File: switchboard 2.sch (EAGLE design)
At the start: 214 parts, among them IC1 MT8816AP, IC10 Z8F2480SO, IC11 LMV321M5, IC12 74HC595D, IC14 74LVC1G125DBV, IC15 74LVC1G125DBV, IC16 LM2940-9, IC17 PC817S OPTO, IC2 NE5532D, IC3 TC7660-SOIC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

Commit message: Layout development.
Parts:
- R14, R16, R18, R19, R2, R24, R3, R7: value 1M SMD -> 1M
- R17, R23, R25, R4: value 1k SMD -> 1k
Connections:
- new net N$83: IC14A.O, R60.1, SJ3.1
- net UART_RX: no longer IC14A.O, R60.1, SJ3.1
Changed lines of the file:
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@@
 <part name="GND2" library="supply1" deviceset="GND" device=""/>
 <part name="IC9" library="linear" deviceset="NE5532" device="D" value="NE5532D"/>
-<part name="R2" library="rcl" deviceset="R-US_" device="R0603" value="1M SMD"/>
-<part name="R3" library="rcl" deviceset="R-US_" device="R0603" value="1M SMD"/>
-<part name="R4" library="rcl" deviceset="R-US_" device="R0603" value="1k SMD"/>
+<part name="R2" library="rcl" deviceset="R-US_" device="R0603" value="1M"/>
+<part name="R3" library="rcl" deviceset="R-US_" device="R0603" value="1M"/>
+<part name="R4" library="rcl" deviceset="R-US_" device="R0603" value="1k"/>
 <part name="GND5" library="supply1" deviceset="GND" device=""/>
 <part name="GND6" library="supply1" deviceset="GND" device=""/>
@@
 <part name="R6" library="rcl" deviceset="R-US_" device="R0805" value="1k SMD"/>
 <part name="GND7" library="supply1" deviceset="GND" device=""/>
-<part name="R7" library="rcl" deviceset="R-US_" device="R0603" value="1M SMD"/>
-<part name="R24" library="rcl" deviceset="R-US_" device="R0603" value="1M SMD"/>
+<part name="R7" library="rcl" deviceset="R-US_" device="R0603" value="1M"/>
+<part name="R24" library="rcl" deviceset="R-US_" device="R0603" value="1M"/>
 <part name="GND50" library="supply1" deviceset="GND" device=""/>
-<part name="R25" library="rcl" deviceset="R-US_" device="R0603" value="1k SMD"/>
+<part name="R25" library="rcl" deviceset="R-US_" device="R0603" value="1k"/>
 <part name="C7" library="rcl" deviceset="C-EU" device="C0603" value="100n"/>
 <part name="R34" library="rcl" deviceset="R-US_" device="R0805" value="100"/>
@@
 <part name="R15" library="rcl" deviceset="R-US_" device="R0805" value="10k"/>
 <part name="IC2" library="linear" deviceset="NE5532" device="D" value="NE5532D"/>
-<part name="R14" library="rcl" deviceset="R-US_" device="R0603" value="1M SMD"/>
-<part name="R16" library="rcl" deviceset="R-US_" device="R0603" value="1M SMD"/>
-<part name="R17" library="rcl" deviceset="R-US_" device="R0603" value="1k SMD"/>
+<part name="R14" library="rcl" deviceset="R-US_" device="R0603" value="1M"/>
+<part name="R16" library="rcl" deviceset="R-US_" device="R0603" value="1M"/>
+<part name="R17" library="rcl" deviceset="R-US_" device="R0603" value="1k"/>
 <part name="GND16" library="supply1" deviceset="GND" device=""/>
 <part name="GND19" library="supply1" deviceset="GND" device=""/>
-<part name="R18" library="rcl" deviceset="R-US_" device="R0603" value="1M SMD"/>
-<part name="R19" library="rcl" deviceset="R-US_" device="R0603" value="1M SMD"/>
+<part name="R18" library="rcl" deviceset="R-US_" device="R0603" value="1M"/>
+<part name="R19" library="rcl" deviceset="R-US_" device="R0603" value="1M"/>
 <part name="GND20" library="supply1" deviceset="GND" device=""/>
-<part name="R23" library="rcl" deviceset="R-US_" device="R0603" value="1k SMD"/>
+<part name="R23" library="rcl" deviceset="R-US_" device="R0603" value="1k"/>
 <part name="C14" library="rcl" deviceset="C-EU" device="C0603" value="100n"/>
 <part name="P_INPUT2" library="pinhead" deviceset="PINHD-1X2" device=""/>
@@
 </segment>
 <segment>
-<wire x1="-347.98" y1="233.68" x2="-342.9" y2="233.68" width="0.1524" layer="91"/>
-<pinref part="IC14" gate="A" pin="O"/>
-<pinref part="SJ3" gate="G$1" pin="1"/>
-<wire x1="-342.9" y1="193.04" x2="-342.9" y2="233.68" width="0.1524" layer="91"/>
-<pinref part="R60" gate="G$1" pin="1"/>
-<wire x1="-335.28" y1="233.68" x2="-342.9" y2="233.68" width="0.1524" layer="91"/>
-<junction x="-342.9" y="233.68"/>
-</segment>
-<segment>
 <pinref part="R60" gate="G$1" pin="2"/>
 <wire x1="-325.12" y1="233.68" x2="-317.5" y2="233.68" width="0.1524" layer="91"/>
@@
 </segment>
 </net>
+<net name="N$83" class="0">
+<segment>
+<pinref part="IC14" gate="A" pin="O"/>
+<pinref part="R60" gate="G$1" pin="1"/>
+<wire x1="-347.98" y1="233.68" x2="-342.9" y2="233.68" width="0.1524" layer="91"/>
+<pinref part="SJ3" gate="G$1" pin="1"/>
+<wire x1="-342.9" y1="233.68" x2="-335.28" y2="233.68" width="0.1524" layer="91"/>
+<wire x1="-342.9" y1="193.04" x2="-342.9" y2="233.68" width="0.1524" layer="91"/>
+<junction x="-342.9" y="233.68"/>
+</segment>
+</net>

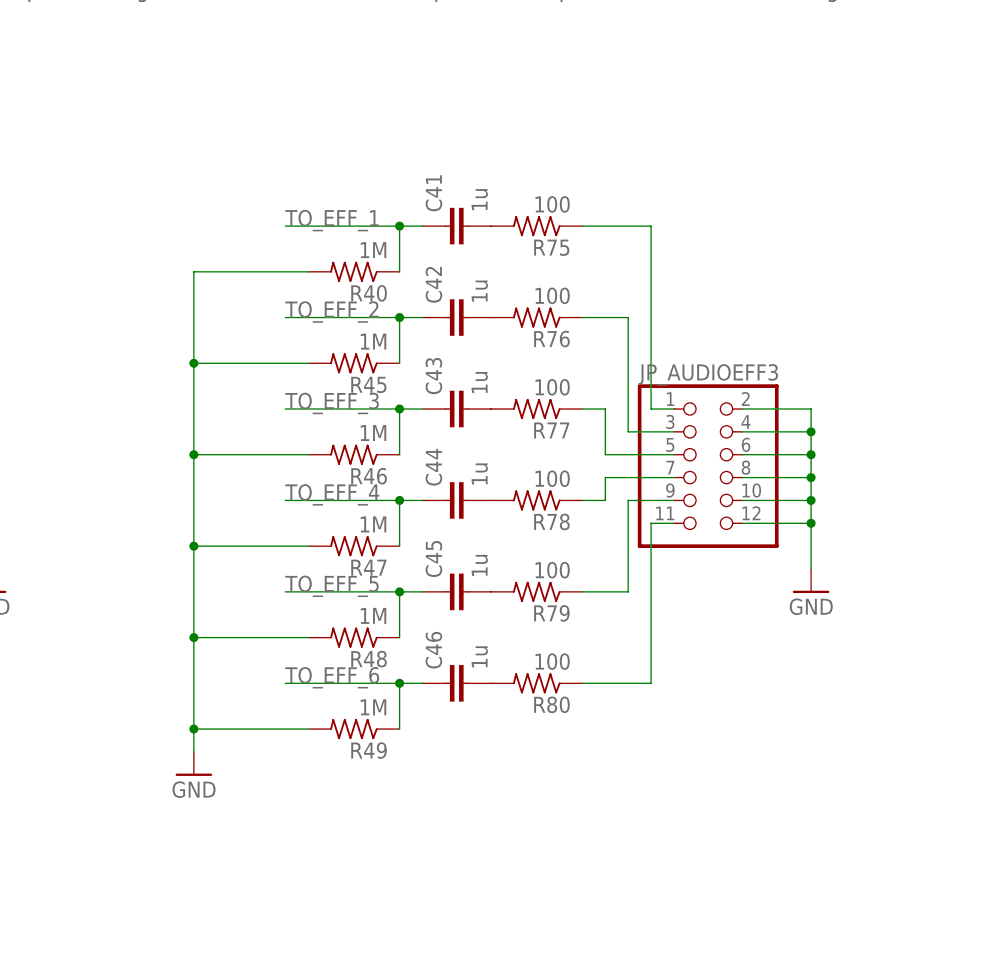
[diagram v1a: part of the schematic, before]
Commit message: Layout development. Board dimensions changed.
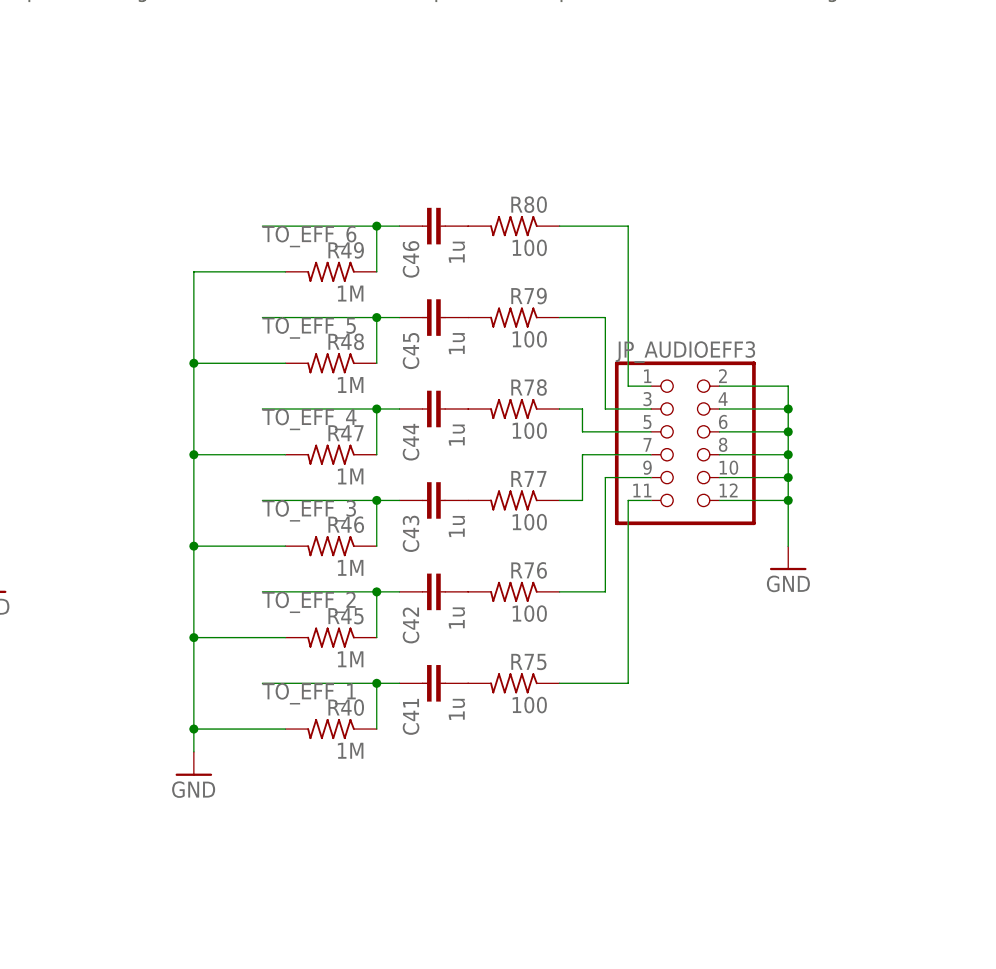
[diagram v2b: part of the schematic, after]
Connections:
- net N$21: now also JP_AUDIOEFF3.11; no longer JP_AUDIOEFF3.1
- net N$32: now also JP_AUDIOEFF3.9; no longer JP_AUDIOEFF3.3
- net N$52: now also JP_AUDIOEFF3.7; no longer JP_AUDIOEFF3.5
- net N$53: now also JP_AUDIOEFF3.5; no longer JP_AUDIOEFF3.7
- net N$59: now also JP_AUDIOEFF3.3; no longer JP_AUDIOEFF3.9
- net N$62: now also JP_AUDIOEFF3.1; no longer JP_AUDIOEFF3.11
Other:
- moved on the sheet: C41, C42, C43, C44, C45, C46, JP_AUDIOEFF3, R40, R45, R46, R47, R48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

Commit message: Layout development. Schematic changes to ease routing process. Some component package changes (mainly from 0805 to 0603).
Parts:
- removed C50, C51: 1u, rcl:C-EUC0603
- removed R51, R52: 1M, rcl:R-US_R0603
- removed R72, R73: 100, rcl:R-US_R0603
- JP_AUDIOEFF1: device pinhead-2:PINHD-2X06_2.54-SMD -> pinhead-2:PINHD-2X03_2.54-SMD
- R15, R34, R6, R60: device rcl:R-US_R0805 -> rcl:R-US_R0603
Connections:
- removed net C_SW3/SCL: IC1.AX2, IC10.PA6/T1IN/!T1OUT!/SCL, P_I2C.2
- removed net FROM_EFF_10: C50.1, IC1.X11, R51.1
- removed net FROM_EFF_11: C51.1, IC1.X12, R52.1
- removed net N$66 (its old number): C50.2, R72.2
- removed net N$67: C51.2, R73.2
- removed net N$70: JP_AUDIOEFF1.9, R13.1
- removed net N$71: JP_AUDIOEFF1.7, R12.1
- new net BTN6/C_SW3: IC1.AX2, IC10.PA1/T0OUT/XOUT
- new net C_SW1/SCL: IC1.AX0, IC10.PA6/T1IN/!T1OUT!/SCL, P_I2C.2
- net BTN6/C_SW1: no longer IC1.AX0, IC10.PA1/T0OUT/XOUT
- net FROM_EFF_4: now also IC1.X6; no longer IC1.X5
- net FROM_EFF_5: now also IC1.X7; no longer IC1.X6
- net FROM_EFF_6: now also IC1.X8; no longer IC1.X7
- net FROM_EFF_7: now also IC1.X9; no longer IC1.X8
- net FROM_EFF_8: now also IC1.X10; no longer IC1.X9
- net FROM_EFF_9: now also IC1.X11; no longer IC1.X10
- net GND: no longer JP_AUDIOEFF1.10, JP_AUDIOEFF1.12, JP_AUDIOEFF1.8, R32.2, R33.2, R36.2, R37.2, R38.2, R51.2, R52.2
- net N$19: now also R32.2, R33.2, R36.2, R37.2, R38.2; no longer JP_AUDIOEFF1.11, R56.1
- net N$73: now also R13.1; no longer R58.1
- net N$74: now also R58.1; no longer R73.1
- net N$75: now also R56.1; no longer R59.1
- net N$76: now also R57.1; no longer R72.1
- net N$9: now also R12.1; no longer R57.1
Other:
- moved on the sheet: C38, C39, C40, C47, C48, C49, R12, R13, R32, R33, R36, R37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

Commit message: Layout development and schematic changes to ease routing process.
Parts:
- C29, C33: device rcl:C-EUC0805 -> rcl:C-EUC0603
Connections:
- removed net BTN6/C_SW1: JP_BTNS2.10, JP_BTNS2.12, JP_BTNS2.8
- net BTN0: now also IC10.PB4/ANA7, JP_BTNS1.6, JP_BTNS1.8, JP_BTNS2.5; no longer IC10.PB1/ANA1/AMPINN, JP_BTNS1.1, JP_BTNS1.7, JP_BTNS2.1
- net BTN1: now also JP_BTNS1.10, JP_BTNS1.4; no longer JP_BTNS1.3, JP_BTNS1.9
- net BTN2: now also JP_BTNS1.12, JP_BTNS1.2, JP_BTNS2.1; no longer JP_BTNS1.11, JP_BTNS1.5, JP_BTNS2.5
- net BTN3: now also IC10.PB1/ANA1/AMPINN, JP_BTNS1.1, JP_BTNS1.3, JP_BTNS1.5; no longer IC10.PB4/ANA7, JP_BTNS1.2, JP_BTNS1.4, JP_BTNS1.6
- net BTN4: now also JP_BTNS1.11, JP_BTNS1.7, JP_BTNS1.9; no longer JP_BTNS1.10, JP_BTNS1.12, JP_BTNS1.8
- net BTN5: now also IC10.PA1/T0OUT/XOUT; no longer IC10.PA0/T0IN/!T0OUT!/XIN
- net BTN6/C_SW3: now also IC10.PA0/T0IN/!T0OUT!/XIN, JP_BTNS2.10, JP_BTNS2.12, JP_BTNS2.8; no longer IC10.PA1/T0OUT/XOUT
- net CS_SHIFT: now also IC10.PA2/DE0/XIN2; no longer IC10.PC3/COUT/LED
- net C_SW2: now also IC10.PC7/LED/T2OUT; no longer IC10.PA2/DE0/XIN2
- net C_SW6: now also IC10.PC3/COUT/LED; no longer IC10.PC6/LED/T2IN/!T2OUT!
- net C_SW7: now also IC10.PC6/LED/T2IN/!T2OUT!; no longer IC10.PC7/LED/T2OUT
- net D+: now also D19.IO2; no longer D19.IO1
- net D-: now also D19.IO1; no longer D19.IO2
- net GND: now also JP_OUTS1.10; no longer JP_OUTS1.9
- net N$44: now also JP_OUTS1.9; no longer JP_OUTS1.10

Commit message: Layout development and schematic changes to ease routing process.
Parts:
- removed IC7: LD117AS33TR, v-reg:LD117AS33TR
- added C50: 100n, rcl:C-EUC0603
- added IC13: REG1117, burr-brown:REG1117
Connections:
- net +3V3: now also IC13.VOUT; no longer IC7.OUT
- net +9V: now also IC13.VIN; no longer IC7.IN
- net -5V: now also C50.1, D1.A, D13.A, D16.A, D8.A; no longer C7.2
- net GND: now also C50.2, C7.2, IC13.GND; no longer D1.A, D13.A, D16.A, D8.A, IC7.ADJ
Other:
- moved on the sheet: C7

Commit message: Layout development.
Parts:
- removed IC13: REG1117, burr-brown:REG1117
- removed P_EXTRA: (no value), pinhead:PINHD-1X5
- added C51: 100n, rcl:C-EUC0603
- added C54, C55: 1u, rcl:C-EUC0603
- added IC7: REG1117, PATSKO:REG1117
- added JP_AUDIOEFF4: (no value), pinhead-2:PINHD-2X03_2.54-SMD
- added R51, R72: 1M, rcl:R-US_R0603
- added R52, R73: 100, rcl:R-US_R0603
- C13, C18, C26: device rcl:C-EUC0805 -> rcl:C-EUC0603
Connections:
- removed net N$35: IC5.TXD, R71.1
- new net FROM_EFF_10: C54.1, IC1.X12, R51.1
- new net FROM_EFF_11: C55.1, IC1.X5, R72.1
- new net N$64: C55.2, R73.2
- new net N$67: JP_AUDIOEFF4.5, R73.1
- new net N$70: JP_AUDIOEFF4.3, R52.1
- new net N$71: JP_AUDIOEFF4.1, R59.1
- new net USB_TO_UART_RX: IC5.TXD, P_UART.2, R71.1
- net +3V3: now also IC7.VOUT; no longer IC13.VOUT
- net +9V: now also C51.1, IC7.VIN; no longer IC13.VIN
- net CS_MEM: no longer P_EXTRA.2
- net CS_SHIFT: no longer P_EXTRA.1
- net C_SW5: no longer P_EXTRA.3
- net C_SW6: no longer P_EXTRA.5
- net C_SW7: no longer P_EXTRA.4
- net GND: now also C51.2, IC7.GND, JP_AUDIOEFF4.2, JP_AUDIOEFF4.4, JP_AUDIOEFF4.6, R32.2, R33.2, R36.2, R37.2, R38.2, R51.2, R72.2; no longer IC13.GND
- net N$19: now also C54.2, R52.2; no longer R32.2, R33.2, R36.2, R37.2, R38.2
- net UART_RX: no longer P_UART.3
- net UART_TX: now also P_UART.3; no longer P_UART.2
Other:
- moved on the sheet: C49, R50, R59, R71

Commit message: Layout development. Ground planes added to top and bottom layers.
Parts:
- removed C14: 100n, rcl:C-EUC0603
- removed P_SPI: (no value), pinhead:PINHD-1X4
- added C56, C57: 100n, rcl:C-EUC0603
- added SJ4: (no value), jumper:SJ
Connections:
- new net N$35: C33.1, IC5.3V3OUT, SJ4.1
- net +3V3: now also SJ4.2; no longer C33.1, IC5.3V3OUT
- net +5V_AN: now also C56.1; no longer C14.1
- net -5V: now also C57.1; no longer C14.2
- net GND: now also C56.2, C57.2; no longer P_SPI.4
- net MISO: no longer P_SPI.1
- net MOSI: no longer P_SPI.2
- net SCK: no longer P_SPI.3

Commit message: Layout development.
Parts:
- JP_OUTS1: device pinhead:PINHD-1X10 -> pinhead:PINHD-1X11
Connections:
- net +3V3: now also JP_OUTS1.1
- net GND: now also JP_OUTS1.11; no longer JP_OUTS1.10
- net N$36: now also JP_OUTS1.2; no longer JP_OUTS1.1
- net N$37: now also JP_OUTS1.3; no longer JP_OUTS1.2
- net N$38: now also JP_OUTS1.4; no longer JP_OUTS1.3
- net N$39: now also JP_OUTS1.5; no longer JP_OUTS1.4
- net N$40: now also JP_OUTS1.6; no longer JP_OUTS1.5
- net N$41: now also JP_OUTS1.7; no longer JP_OUTS1.6
- net N$42: now also JP_OUTS1.8; no longer JP_OUTS1.7
- net N$43: now also JP_OUTS1.9; no longer JP_OUTS1.8
- net N$44: now also JP_OUTS1.10; no longer JP_OUTS1.9
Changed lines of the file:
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@@
 <part name="D6" library="LUIS" deviceset="SS14" device=""/>
 <part name="GND78" library="supply1" deviceset="GND" device=""/>
-<part name="JP_OUTS1" library="pinhead" deviceset="PINHD-1X10" device=""/>
 <part name="GND81" library="supply1" deviceset="GND" device=""/>
 <part name="GND82" library="supply1" deviceset="GND" device=""/>
@@
 <part name="GND100" library="supply1" deviceset="GND" device=""/>
 <part name="SJ4" library="jumper" deviceset="SJ" device=""/>
+<part name="JP_OUTS1" library="pinhead" library_urn="urn:adsk.eagle:library:325" deviceset="PINHD-1X11" device="" package3d_urn="urn:adsk.eagle:package:22410/1"/>
+<part name="U$2" library="supply1" deviceset="+3V3" device=""/>
 </parts>
 <sheets>
@@
 <instance part="D6" gate="G$1" x="60.96" y="228.6" rot="MR0"/>
 <instance part="GND78" gate="1" x="101.6" y="-48.26" rot="MR0"/>
-<instance part="JP_OUTS1" gate="A" x="393.7" y="45.72"/>
-<instance part="GND81" gate="1" x="381" y="33.02" rot="R270"/>
+<instance part="GND81" gate="1" x="383.54" y="30.48"/>
 <instance part="GND82" gate="1" x="-38.1" y="-370.84"/>
 <instance part="IC12" gate="P" x="340.36" y="7.62"/>
@@
 <instance part="GND100" gate="1" x="96.52" y="-294.64"/>
 <instance part="SJ4" gate="1" x="-365.76" y="91.44" rot="MR0"/>
+<instance part="JP_OUTS1" gate="A" x="393.7" y="45.72"/>
+<instance part="U$2" gate="G$1" x="383.54" y="60.96" smashed="yes">
+<attribute name="VALUE" x="386.08" y="60.96" size="1.778" layer="96" rot="R90"/>
+</instance>
 </instances>
 <busses>
@@
 <wire x1="-370.84" y1="91.44" x2="-375.92" y2="91.44" width="0.1524" layer="91"/>
 </segment>
+<segment>
+<pinref part="JP_OUTS1" gate="A" pin="1"/>
+<pinref part="U$2" gate="G$1" pin="+3V3"/>
+<wire x1="383.54" y1="58.42" x2="391.16" y2="58.42" width="0.1524" layer="91"/>
+</segment>
 </net>
 <net name="GND" class="0">
@@
 <segment>
 <pinref part="GND81" gate="1" pin="GND"/>
-<pinref part="JP_OUTS1" gate="A" pin="10"/>
 <wire x1="383.54" y1="33.02" x2="391.16" y2="33.02" width="0.1524" layer="91"/>
+<pinref part="JP_OUTS1" gate="A" pin="11"/>
 </segment>
 <segment>
@@
 <segment>
 <pinref part="R61" gate="G$1" pin="1"/>
-<pinref part="JP_OUTS1" gate="A" pin="1"/>
 <wire x1="378.46" y1="55.88" x2="391.16" y2="55.88" width="0.1524" layer="91"/>
+<pinref part="JP_OUTS1" gate="A" pin="2"/>
 </segment>
 </net>
 <net name="N$37" class="0">
 <segment>
-<pinref part="JP_OUTS1" gate="A" pin="2"/>
 <pinref part="R62" gate="G$1" pin="1"/>
 <wire x1="391.16" y1="53.34" x2="363.22" y2="53.34" width="0.1524" layer="91"/>
+<pinref part="JP_OUTS1" gate="A" pin="3"/>
 </segment>
 </net>
@@
 <segment>
 <pinref part="R63" gate="G$1" pin="1"/>
-<pinref part="JP_OUTS1" gate="A" pin="3"/>
 <wire x1="378.46" y1="50.8" x2="391.16" y2="50.8" width="0.1524" layer="91"/>
+<pinref part="JP_OUTS1" gate="A" pin="4"/>
 </segment>
 </net>
 <net name="N$39" class="0">
 <segment>
-<pinref part="JP_OUTS1" gate="A" pin="4"/>
 <pinref part="R64" gate="G$1" pin="1"/>
 <wire x1="391.16" y1="48.26" x2="363.22" y2="48.26" width="0.1524" layer="91"/>
+<pinref part="JP_OUTS1" gate="A" pin="5"/>
 </segment>
 </net>
@@
 <segment>
 <pinref part="R65" gate="G$1" pin="1"/>
-<pinref part="JP_OUTS1" gate="A" pin="5"/>
 <wire x1="378.46" y1="45.72" x2="391.16" y2="45.72" width="0.1524" layer="91"/>
+<pinref part="JP_OUTS1" gate="A" pin="6"/>
 </segment>
 </net>
 <net name="N$41" class="0">
 <segment>
-<pinref part="JP_OUTS1" gate="A" pin="6"/>
 <pinref part="R66" gate="G$1" pin="1"/>
 <wire x1="391.16" y1="43.18" x2="363.22" y2="43.18" width="0.1524" layer="91"/>
+<pinref part="JP_OUTS1" gate="A" pin="7"/>
 </segment>
 </net>
@@
 <segment>
 <pinref part="R67" gate="G$1" pin="1"/>
-<pinref part="JP_OUTS1" gate="A" pin="7"/>
 <wire x1="378.46" y1="40.64" x2="391.16" y2="40.64" width="0.1524" layer="91"/>
+<pinref part="JP_OUTS1" gate="A" pin="8"/>
 </segment>
 </net>
 <net name="N$43" class="0">
 <segment>
-<pinref part="JP_OUTS1" gate="A" pin="8"/>
 <pinref part="R68" gate="G$1" pin="1"/>
 <wire x1="391.16" y1="38.1" x2="363.22" y2="38.1" width="0.1524" layer="91"/>
+<pinref part="JP_OUTS1" gate="A" pin="9"/>
 </segment>
 </net>
@@
 <net name="N$44" class="0">
 <segment>
-<pinref part="JP_OUTS1" gate="A" pin="9"/>
 <wire x1="391.16" y1="35.56" x2="368.3" y2="35.56" width="0.1524" layer="91"/>
 <wire x1="368.3" y1="35.56" x2="368.3" y2="33.02" width="0.1524" layer="91"/>
 <pinref part="IC12" gate="A" pin="QH*"/>
 <wire x1="368.3" y1="33.02" x2="353.06" y2="33.02" width="0.1524" layer="91"/>
+<pinref part="JP_OUTS1" gate="A" pin="10"/>
 </segment>
 </net>
@@
 will not be understood (or retained) with this version.
 </note>
+<note version="8.3" severity="warning">
+Since Version 8.3, EAGLE supports the association of 3D packages
+with devices in libraries, schematics, and board files. Those 3D
+packages will not be understood (or retained) with this version.
+</note>
 </compatibility>
